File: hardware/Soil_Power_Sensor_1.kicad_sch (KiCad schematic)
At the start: 24 parts, among them J1 Screw_Terminal_01x05, J4 Rsense, U1 THS4532, U2 MAX9944, U3 INA296A, U4 ADS1219

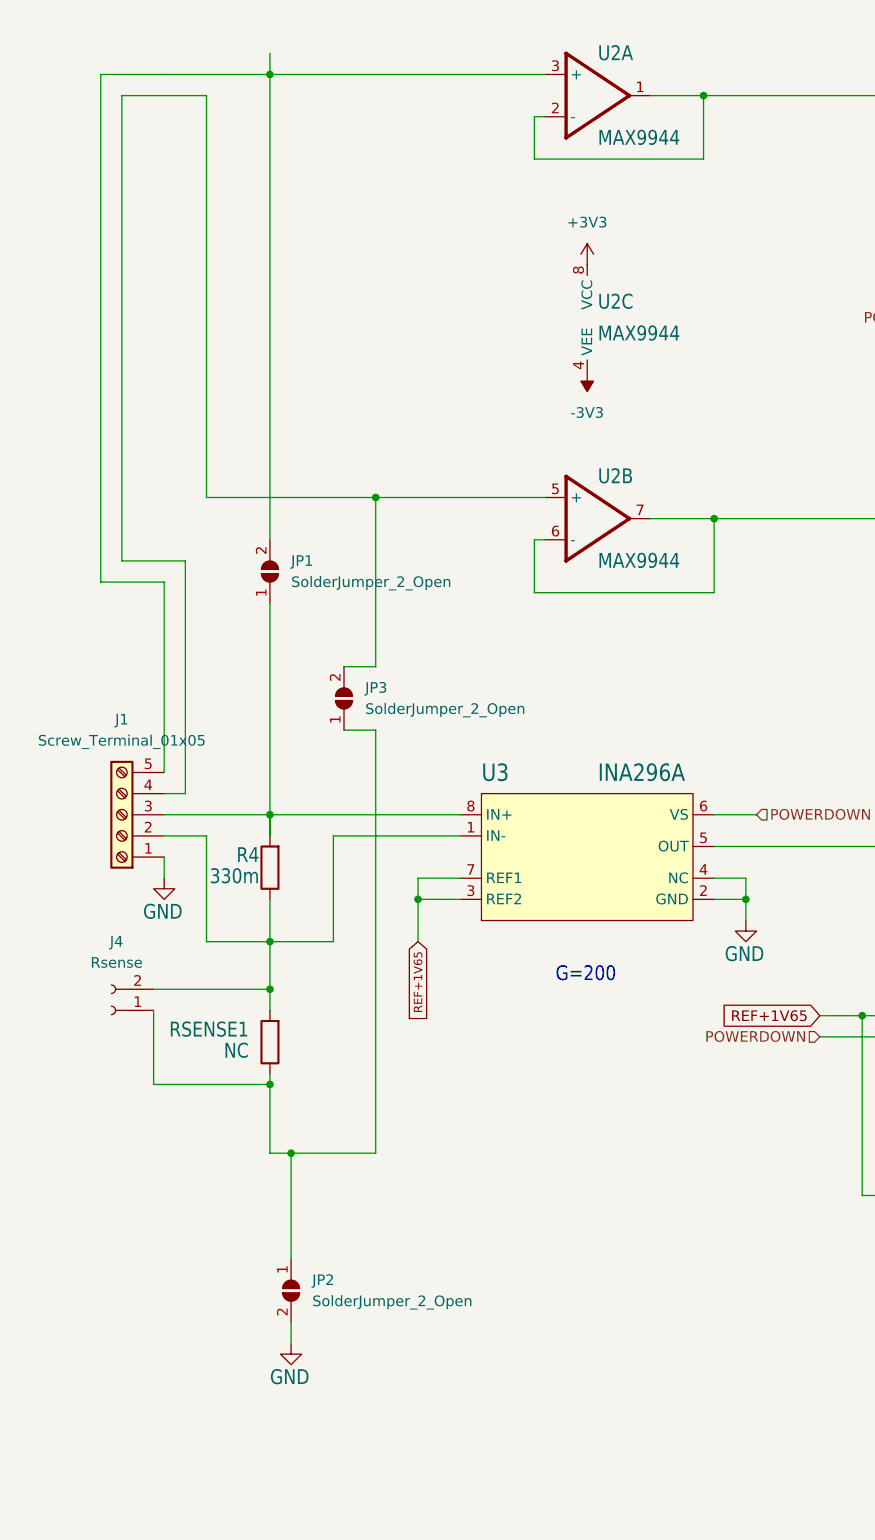
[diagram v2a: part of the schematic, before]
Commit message: Updated screw terminal
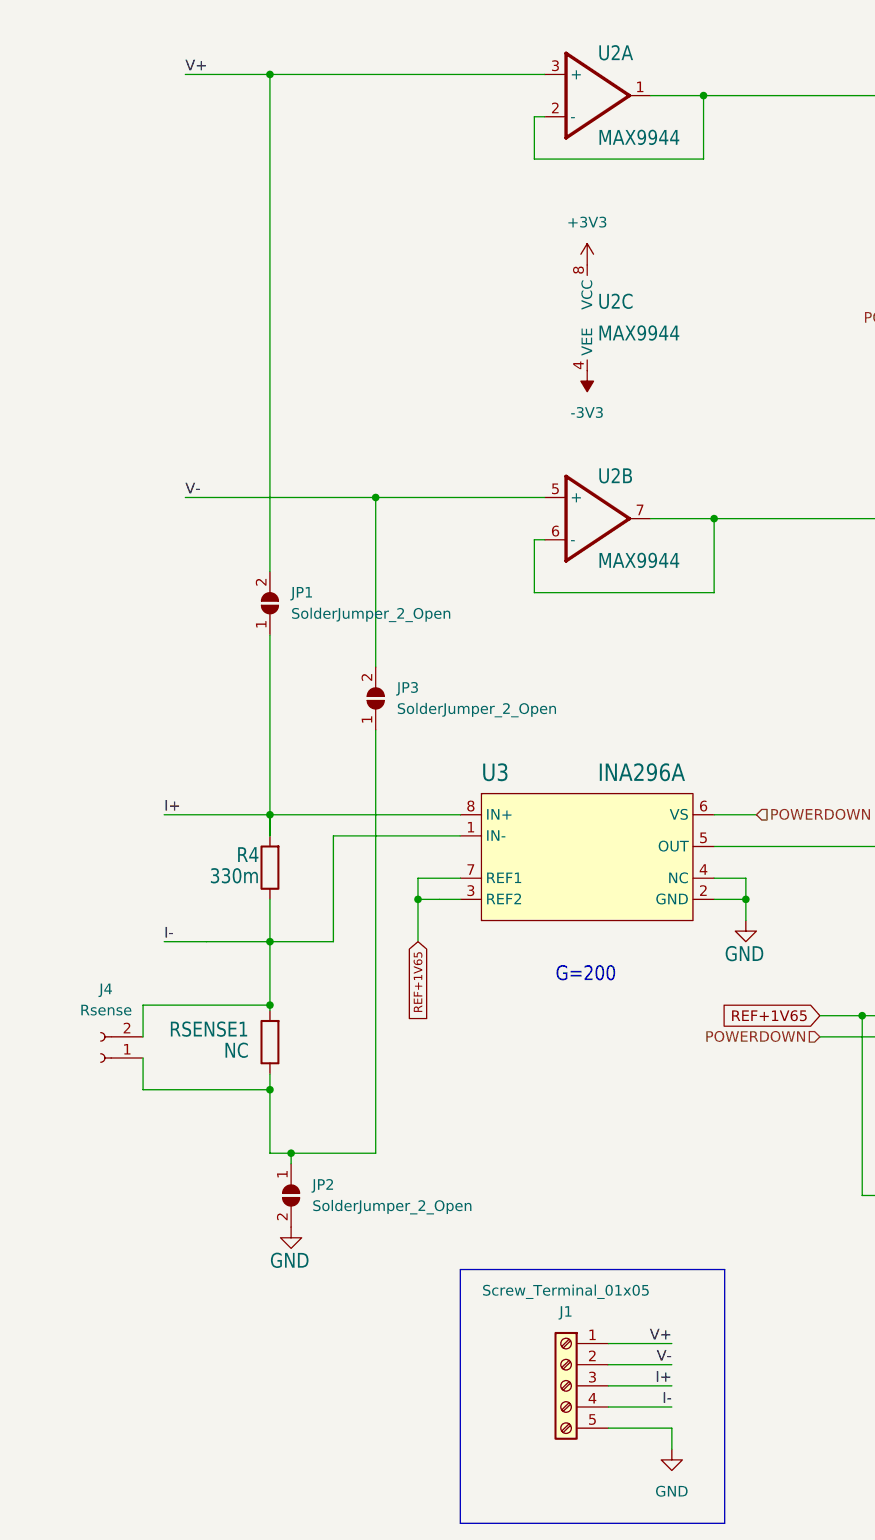
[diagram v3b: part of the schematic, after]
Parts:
- J1: footprint TerminalBlock_WAGO:TerminalBlock_WAGO_236-205_1x05_P7.50mm_45Degree -> TerminalBlock_Phoenix:TerminalBlock_Phoenix_PT-1,5-5-5.0-H_1x05_P5.00mm_Horizontal; MFC (none) -> Phoenix Contact; MPN (none) -> 1935190; REF (none) -> https://www.digikey.com/en/products/detail/phoenix-contact/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
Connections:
- net GND: now also J1.5 (Pin_5); no longer J1.1 (Pin_1)
- net V-: now reaches JP3.2 (B), U2.5 (+)
- net V-: now also J1.2 (Pin_2); no longer J1.4 (Pin_4)
- net I-: now reaches J4.2 (Pin_2), R4.1, RSENSE1.2, U3.1 (IN-)
- net I-: now also J1.4 (Pin_4); no longer J1.2 (Pin_2)
- net I+: now reaches J1.3 (Pin_3), JP1.1 (A), R4.2, U3.8 (IN+)
- net V+: now reaches JP1.2 (B), U2.3 (+)
- net V+: now also J1.1 (Pin_1); no longer J1.5 (Pin_5)
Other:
- moved on the sheet: J4, JP1, JP2, JP3

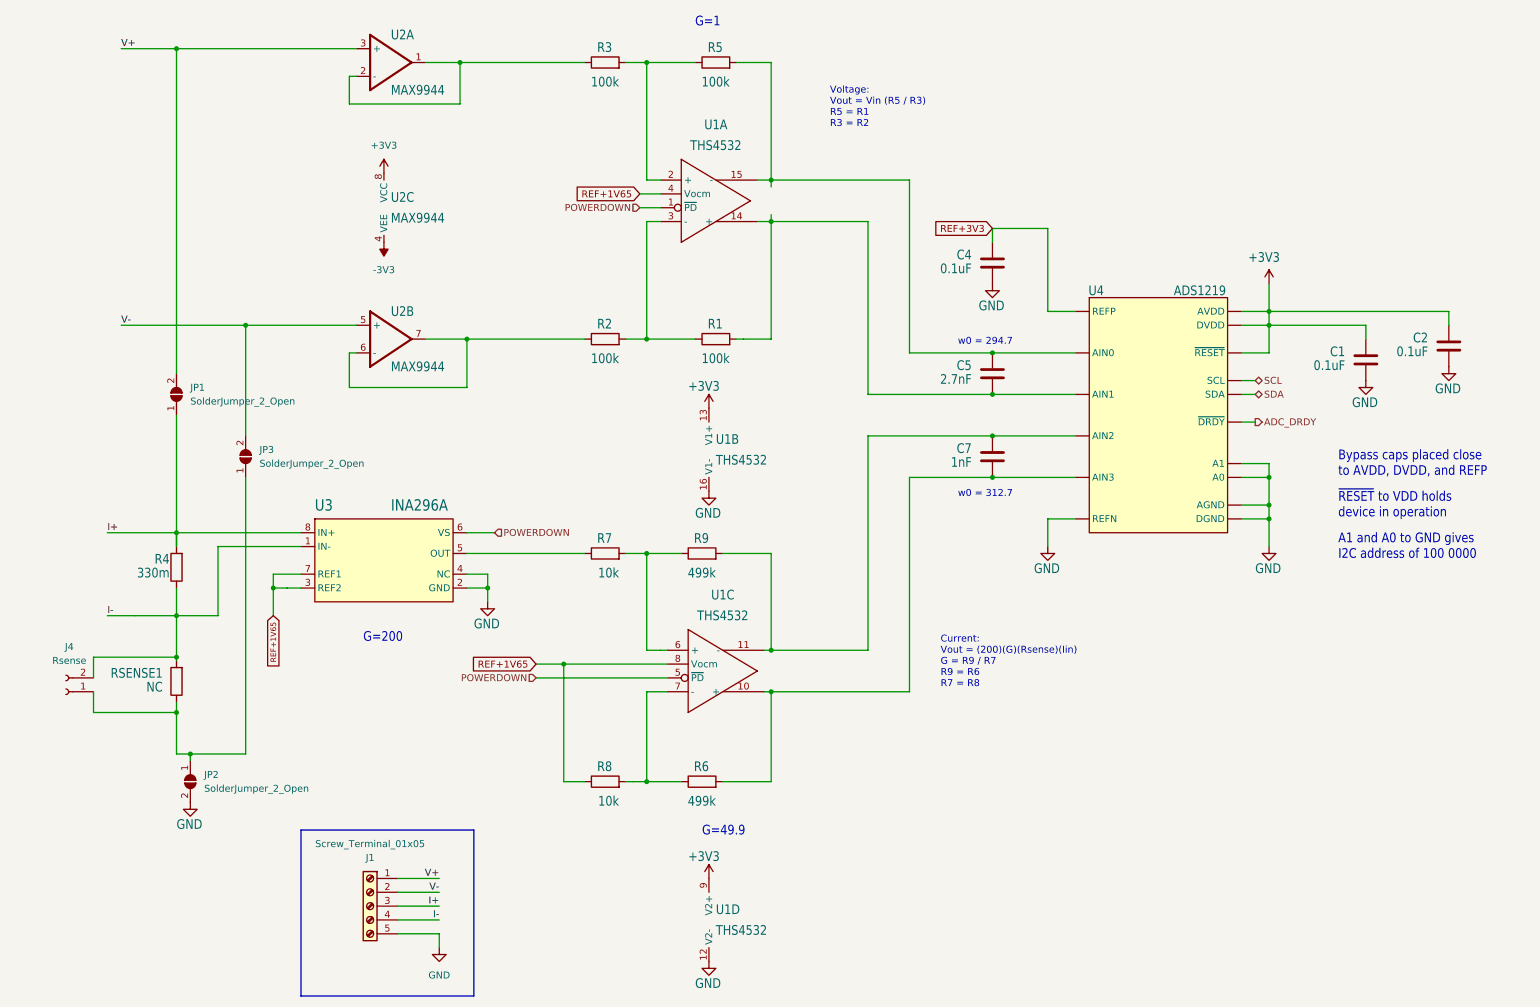
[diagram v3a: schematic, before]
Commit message: Fixed ERC errors
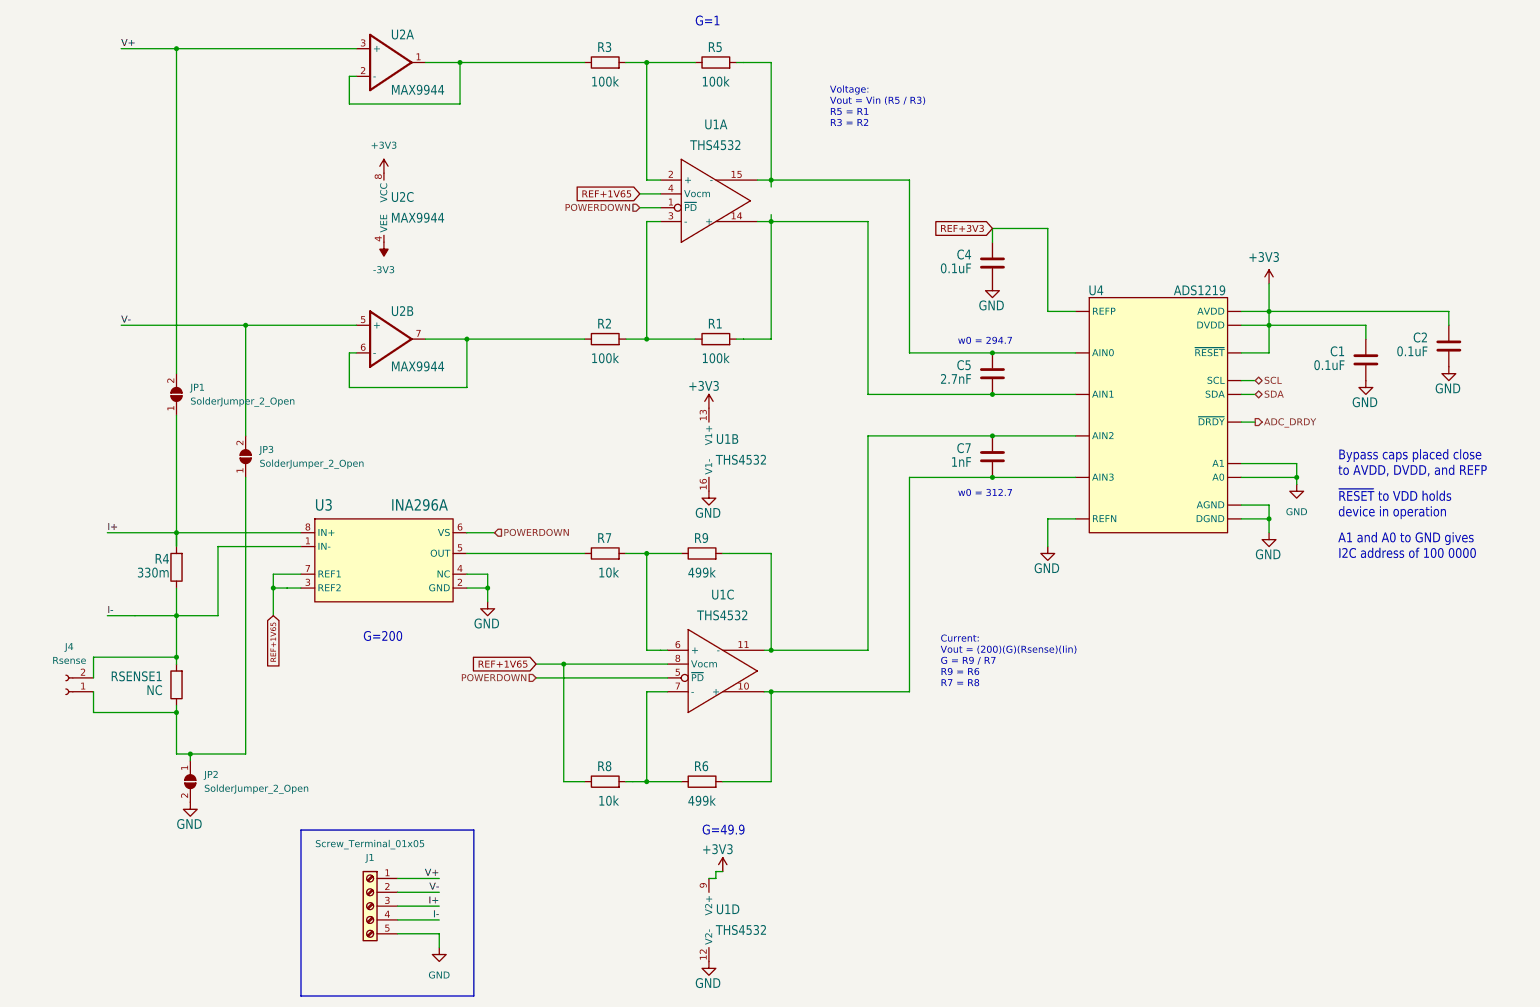
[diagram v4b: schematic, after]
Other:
- moved on the sheet: RSENSE1
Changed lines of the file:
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@@
   (junction (at 236.22 106.68) (diameter 0) (color 0 0 0 0)
   )
-  (junction (at 236.22 104.14) (diameter 0) (color 0 0 0 0)
-  )
   (junction (at 185.42 76.2) (diameter 0) (color 0 0 0 0)
   )
+  (junction (at 241.3 99.06) (diameter 0) (color 0 0 0 0)
+  )
   (junction (at 121.92 113.03) (diameter 0) (color 0 0 0 0)
   )
@@
   (junction (at 185.42 83.82) (diameter 0) (color 0 0 0 0)
   )
-  (junction (at 236.22 99.06) (diameter 0) (color 0 0 0 0)
-  )
   (junction (at 144.78 130.81) (diameter 0) (color 0 0 0 0)
   )
@@
     (stroke (width 0.1524) (type solid))
   )
+  (wire (pts (xy 241.3 99.06) (xy 241.3 100.33))
+    (stroke (width 0) (type default))
+  )
   (wire (pts (xy 118.11 154.94) (xy 119.38 154.94))
     (stroke (width 0) (type default))
@@
     (stroke (width 0) (type default))
   )
-  (wire (pts (xy 35.56 132.08) (xy 35.56 132.715))
+  (wire (pts (xy 134.62 171.45) (xy 134.62 172.72))
+    (stroke (width 0) (type default))
+  )
+  (wire (pts (xy 35.56 132.08) (xy 35.56 133.35))
     (stroke (width 0.1524) (type solid))
   )
@@
     (stroke (width 0.1524) (type solid))
   )
-  (wire (pts (xy 236.22 96.52) (xy 236.22 99.06))
+  (wire (pts (xy 241.3 96.52) (xy 241.3 99.06))
     (stroke (width 0.1524) (type solid))
   )
@@
     (stroke (width 0.1524) (type solid))
   )
+  (wire (pts (xy 134.62 172.72) (xy 133.35 172.72))
+    (stroke (width 0) (type default))
+  )
   (wire (pts (xy 236.22 68.58) (xy 269.24 68.58))
     (stroke (width 0.1524) (type solid))
@@
     (stroke (width 0.1524) (type solid))
   )
+  (wire (pts (xy 135.89 171.45) (xy 134.62 171.45))
+    (stroke (width 0) (type default))
+  )
   (wire (pts (xy 53.34 116.84) (xy 53.34 119.38))
     (stroke (width 0.1524) (type solid))
   )
-  (wire (pts (xy 231.14 99.06) (xy 236.22 99.06))
+  (wire (pts (xy 231.14 99.06) (xy 241.3 99.06))
     (stroke (width 0.1524) (type solid))
   )
@@
     (stroke (width 0.1524) (type solid))
   )
-  (wire (pts (xy 35.56 140.335) (xy 35.56 142.24))
+  (wire (pts (xy 35.56 140.97) (xy 35.56 142.24))
     (stroke (width 0.1524) (type solid))
   )
@@
     (stroke (width 0.1524) (type solid))
   )
-  (wire (pts (xy 236.22 99.06) (xy 236.22 104.14))
-    (stroke (width 0.1524) (type solid))
-  )
   (wire (pts (xy 119.38 154.94) (xy 121.92 154.94))
     (stroke (width 0.1524) (type solid))
@@
     (stroke (width 0.1524) (type solid))
   )
-  (wire (pts (xy 231.14 96.52) (xy 236.22 96.52))
+  (wire (pts (xy 231.14 96.52) (xy 241.3 96.52))
     (stroke (width 0.1524) (type solid))
   )
@@
     (stroke (width 0.1524) (type solid))
   )
-  (wire (pts (xy 236.22 106.68) (xy 236.22 111.76))
+  (wire (pts (xy 236.22 106.68) (xy 236.22 109.22))
     (stroke (width 0.1524) (type solid))
   )
@@
   (hierarchical_label "POWERDOWN" (shape input) (at 120.65 49.53 180) (fields_autoplaced)
     (effects (font (size 1.27 1.27)) (justify right))
+  )
+  (symbol (lib_id "power:GND") (at 241.3 100.33 0) (unit 1)
+    (in_bom yes) (on_board yes) (dnp no) (fields_autoplaced)
+    (property "Reference" "#PWR016" (at 241.3 106.68 0)
+      (effects (font (size 1.27 1.27)) hide)
+    )
+    (property "Value" "GND" (at 241.3 105.41 0)
+      (effects (font (size 1.27 1.27)))
+    )
+    (property "Footprint" "" (at 241.3 100.33 0)
+      (effects (font (size 1.27 1.27)) hide)
+    )
+    (property "Datasheet" "" (at 241.3 100.33 0)
+      (effects (font (size 1.27 1.27)) hide)
+    )
+    (pin "1")
+    (instances
+      (project "Soil Power Sensor"
+        (path "/5300ec4d-4648-40a1-8d89-4fa6b3bf32a3/643deee0-b2c1-47dd-8bbd-6697ae8f1315"
+          (reference "#PWR016") (unit 1)
+        )
+      )
+    )
   )
   (symbol (lib_id "Jumper:SolderJumper_2_Open") (at 38.1 154.94 270) (unit 1)
@@
     )
   )
-  (symbol (lib_id "power:GND") (at 236.22 111.76 0) (unit 1)
-    (in_bom yes) (on_board yes) (dnp no)
-    (property "Reference" "#GND08" (at 236.22 111.76 0)
-      (effects (font (size 1.27 1.27)) hide)
-    )
-    (property "Value" "GND" (at 233.68 116.84 0)
-      (effects (font (size 1.778 1.5113)) (justify left bottom))
-    )
-    (property "Footprint" "" (at 236.22 111.76 0)
-      (effects (font (size 1.27 1.27)) hide)
-    )
-    (property "Datasheet" "" (at 236.22 111.76 0)
+  (symbol (lib_id "power:GND") (at 236.22 109.22 0) (unit 1)
+    (in_bom yes) (on_board yes) (dnp no)
+    (property "Reference" "#GND08" (at 236.22 109.22 0)
+      (effects (font (size 1.27 1.27)) hide)
+    )
+    (property "Value" "GND" (at 233.68 114.3 0)
+      (effects (font (size 1.778 1.5113)) (justify left bottom))
+    )
+    (property "Footprint" "" (at 236.22 109.22 0)
+      (effects (font (size 1.27 1.27)) hide)
+    )
+    (property "Datasheet" "" (at 236.22 109.22 0)
       (effects (font (size 1.27 1.27)) hide)
     )
@@
     )
   )
-  (symbol (lib_id "power:+3V3") (at 133.35 172.72 0) (unit 1)
-    (in_bom yes) (on_board yes) (dnp no)
-    (property "Reference" "#+3V02" (at 133.35 172.72 0)
-      (effects (font (size 1.27 1.27)) hide)
-    )
-    (property "Value" "+3V3" (at 129.54 167.64 0)
+  (symbol (lib_id "power:+3V3") (at 135.89 171.45 0) (unit 1)
+    (in_bom yes) (on_board yes) (dnp no)
+    (property "Reference" "#+3V02" (at 135.89 171.45 0)
+      (effects (font (size 1.27 1.27)) hide)
+    )
+    (property "Value" "+3V3" (at 132.08 166.37 0)
       (effects (font (size 1.778 1.5113)) (justify left top))
     )
-    (property "Footprint" "" (at 133.35 172.72 0)
-      (effects (font (size 1.27 1.27)) hide)
-    )
-    (property "Datasheet" "" (at 133.35 172.72 0)
+    (property "Footprint" "" (at 135.89 171.45 0)
+      (effects (font (size 1.27 1.27)) hide)
+    )
+    (property "Datasheet" "" (at 135.89 171.45 0)
       (effects (font (size 1.27 1.27)) hide)
     )
@@
     )
   )
-  (symbol (lib_id "Device:R") (at 35.56 136.525 180) (unit 1)
-    (in_bom yes) (on_board yes) (dnp no)
-    (property "Reference" "RSENSE1" (at 33.02 133.985 0)
-      (effects (font (size 1.778 1.5113)) (justify left bottom))
-    )
-    (property "Value" "NC" (at 33.02 136.525 0)
-      (effects (font (size 1.778 1.5113)) (justify left bottom))
-    )
-    (property "Footprint" "Resistor_SMD:R_0603_1608Metric" (at 37.338 136.525 90)
-      (effects (font (size 1.27 1.27)) hide)
-    )
-    (property "Datasheet" "~" (at 35.56 136.525 0)
-      (effects (font (size 1.27 1.27)) hide)
-    )
+  (symbol (lib_id "Device:R") (at 35.56 137.16 180) (unit 1)
+    (in_bom yes) (on_board yes) (dnp no)
+    (property "Reference" "RSENSE1" (at 33.02 134.62 0)
+      (effects (font (size 1.778 1.5113)) (justify left bottom))
+    )
+    (property "Value" "NC" (at 33.02 137.16 0)
+      (effects (font (size 1.778 1.5113)) (justify left bottom))
+    )
+    (property "Footprint" "Resistor_SMD:R_0603_1608Metric" (at 37.338 137.16 90)
+      (effects (font (size 1.27 1.27)) hide)
+    )
+    (property "Datasheet" "~" (at 35.56 137.16 0)
+      (effects (font (size 1.27 1.27)) hide)
+    )
